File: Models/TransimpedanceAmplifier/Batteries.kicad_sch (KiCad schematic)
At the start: 8 parts

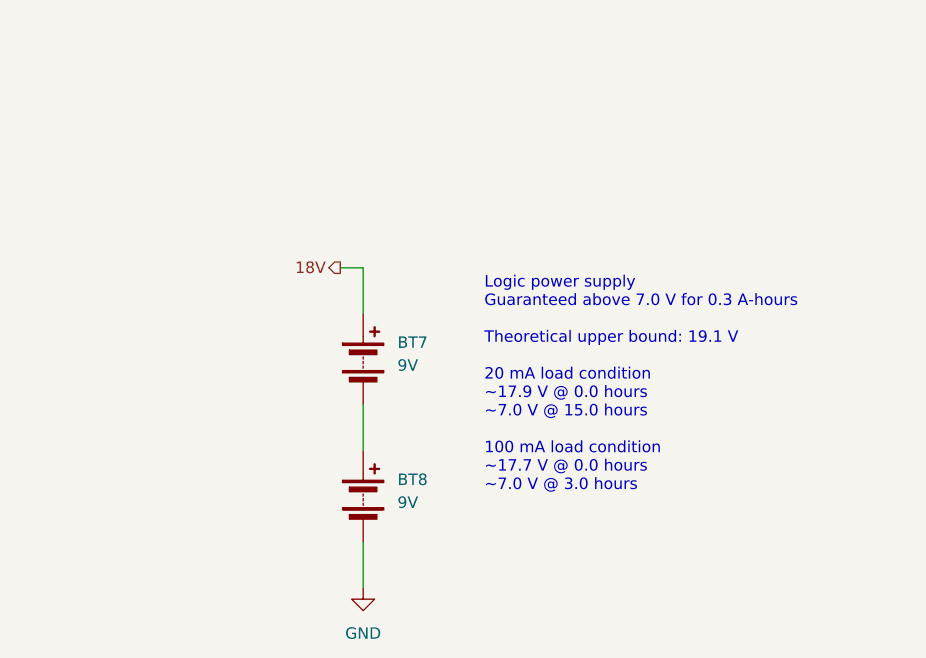
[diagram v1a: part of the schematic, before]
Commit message: Corrected some errors in the power calculations
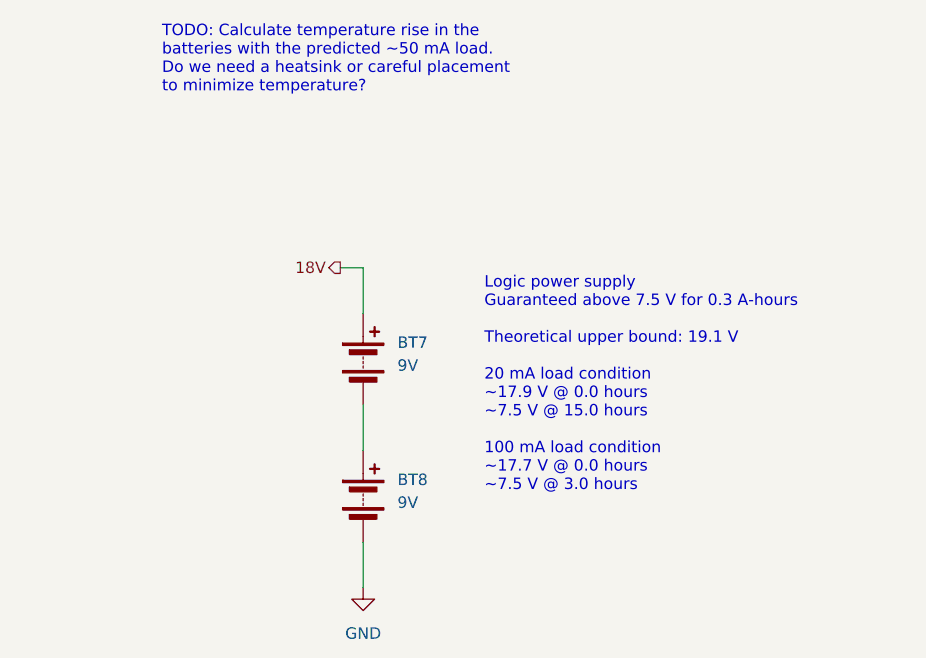
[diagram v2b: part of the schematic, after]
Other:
- note added: "Logic power supply Guaranteed above 7.5 V for 0.3 A-hours Theoretical upper bound: 19.1 V 20 mA load condition ~17.9 V @ 0.0 hours ~7.5 V @ 15.0 hours 100 mA load condition ~17.7 V @ 0.0 hours ~7.5 V @ 3.0 hours"
- note added: "TODO: Calculate temperature rise in the batteries with the predicted ~50 mA load. Do we need a heatsink or careful placement to minimize temperature?"
- note removed: "Logic power supply Guaranteed above 7.0 V for 0.3 A-hours Theoretical upper bound: 19.1 V 20 mA load condition ~17.9 V @ 0.0 hours ~7.0 V @ 15.0 hours 100 mA load condition ~17.7 V @ 0.0 hours ~7.0 V @ 3.0 hours"
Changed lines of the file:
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@@
 		)
 	)
-	(text "Logic power supply\nGuaranteed above 7.0 V for 0.3 A-hours\n\nTheoretical upper bound: 19.1 V\n\n20 mA load condition\n~17.9 V @ 0.0 hours\n~7.0 V @ 15.0 hours\n\n100 mA load condition\n~17.7 V @ 0.0 hours\n~7.0 V @ 3.0 hours"
+	(text "TODO: Calculate temperature rise in the\nbatteries with the predicted ~50 mA load.\nDo we need a heatsink or careful placement\nto minimize temperature?"
+		(exclude_from_sim no)
+		(at 142.748 39.116 0)
+		(effects
+			(font
+				(size 1.27 1.27)
+			)
+			(justify left top)
+		)
+	)
+	(text "Logic power supply\nGuaranteed above 7.5 V for 0.3 A-hours\n\nTheoretical upper bound: 19.1 V\n\n20 mA load condition\n~17.9 V @ 0.0 hours\n~7.5 V @ 15.0 hours\n\n100 mA load condition\n~17.7 V @ 0.0 hours\n~7.5 V @ 3.0 hours"
 		(exclude_from_sim no)
 		(at 178.562 67.056 0)

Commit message: Save progress
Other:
- note added: "Power / Thermal Concerns Internal resistance: 1-2 Ω per battery Maximum current load: 50 mA I2R power dissipation: 5 mW per battery"
- note removed: "TODO: Calculate temperature rise in the batteries with the predicted ~50 mA load. Do we need a heatsink or careful placement to minimize temperature?"
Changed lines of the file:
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@@
 		)
 	)
-	(text "TODO: Calculate temperature rise in the\nbatteries with the predicted ~50 mA load.\nDo we need a heatsink or careful placement\nto minimize temperature?"
+	(text "Logic power supply\nGuaranteed above 7.5 V for 0.3 A-hours\n\nTheoretical upper bound: 19.1 V\n\n20 mA load condition\n~17.9 V @ 0.0 hours\n~7.5 V @ 15.0 hours\n\n100 mA load condition\n~17.7 V @ 0.0 hours\n~7.5 V @ 3.0 hours"
 		(exclude_from_sim no)
-		(at 142.748 39.116 0)
+		(at 178.562 67.056 0)
 		(effects
 			(font
@@
 		)
 	)
-	(text "Logic power supply\nGuaranteed above 7.5 V for 0.3 A-hours\n\nTheoretical upper bound: 19.1 V\n\n20 mA load condition\n~17.9 V @ 0.0 hours\n~7.5 V @ 15.0 hours\n\n100 mA load condition\n~17.7 V @ 0.0 hours\n~7.5 V @ 3.0 hours"
+	(text "Power / Thermal Concerns\n\nInternal resistance: 1-2 Ω per battery\nMaximum current load: 50 mA\nI2R power dissipation: 5 mW per battery"
 		(exclude_from_sim no)
-		(at 178.562 67.056 0)
+		(at 152.908 26.67 0)
 		(effects
 			(font

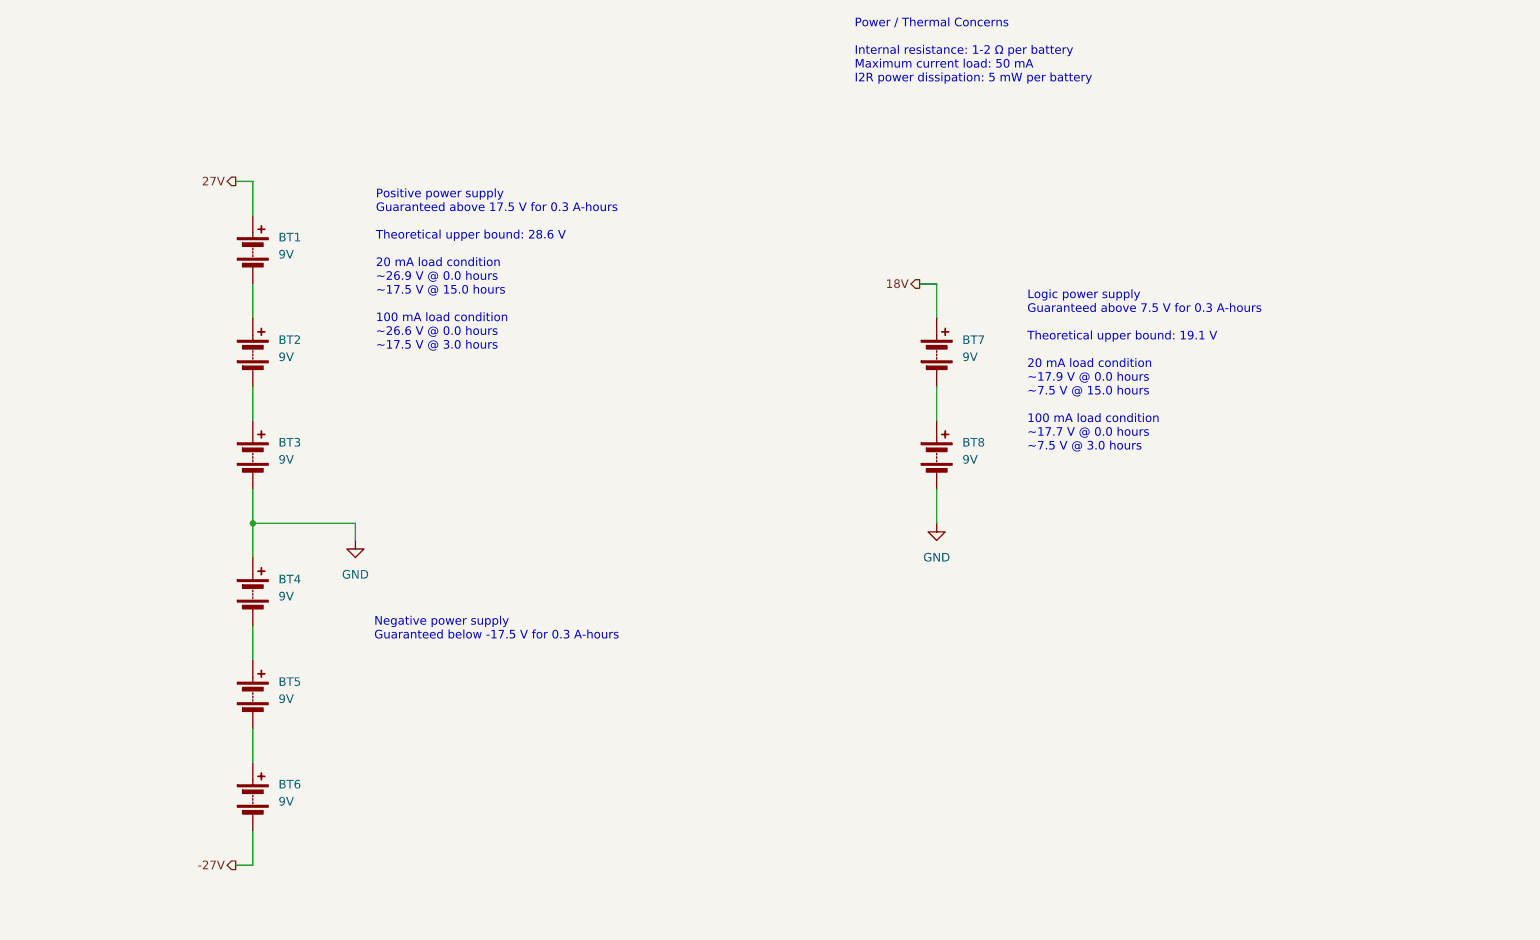
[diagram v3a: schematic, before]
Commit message: Improved the power supply schematic
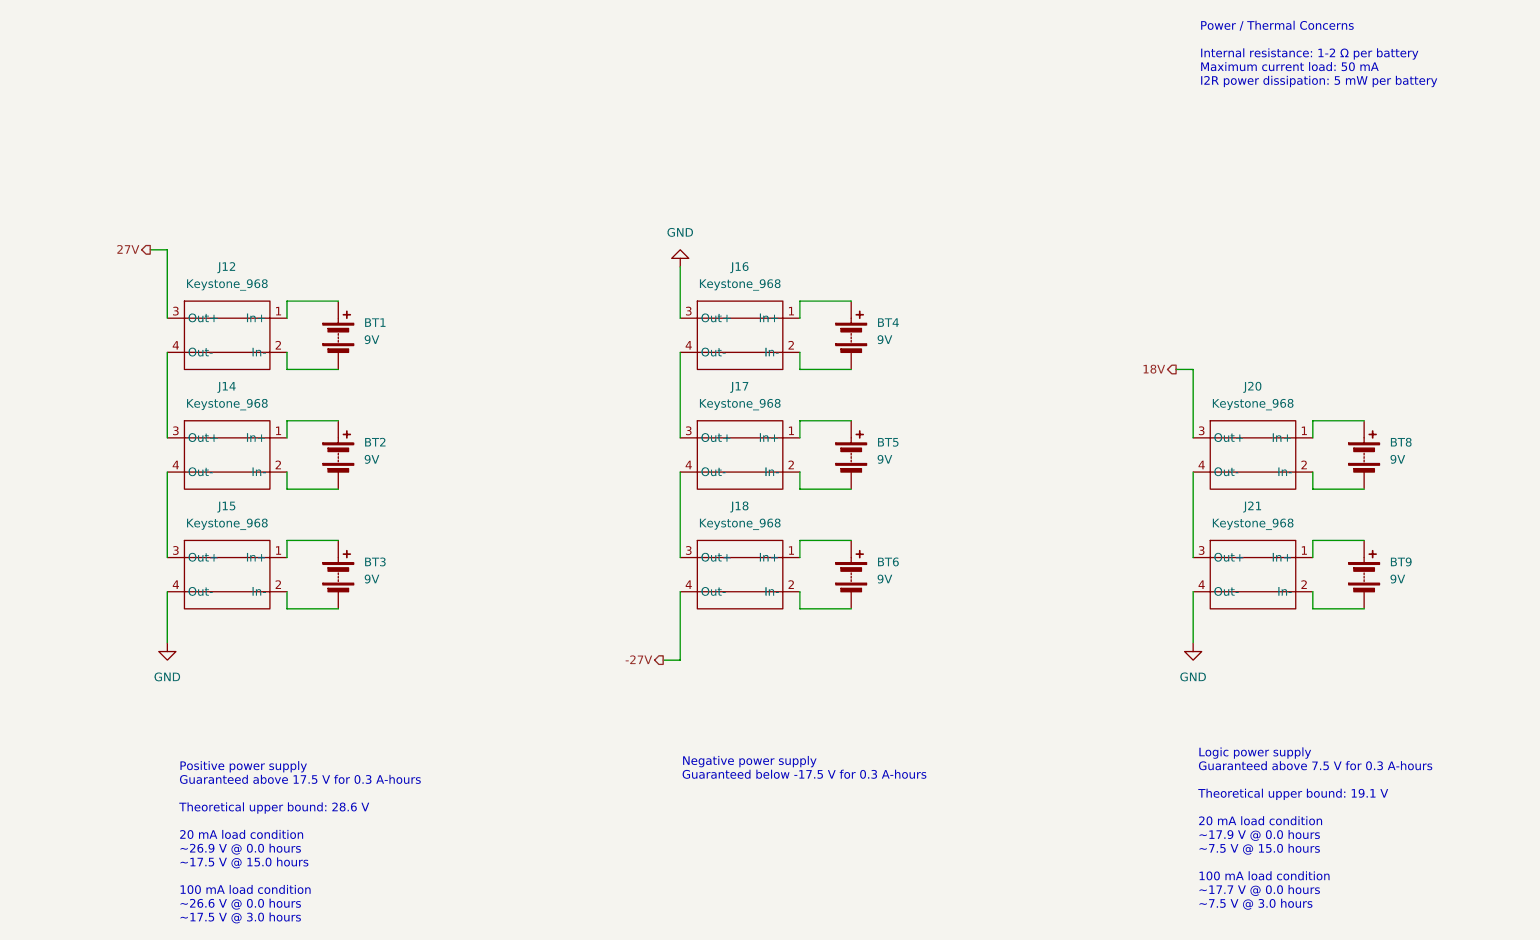
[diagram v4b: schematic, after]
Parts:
- removed BT7: 9V, symbol Device:Battery
- added BT9: 9V, symbol Device:Battery
- added J12, J14, J15, J16, J17, J18, J20, J21: Keystone_968, symbol Custom:Keystone_968
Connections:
- net -27V: now also J18.4 (Out-); no longer BT6.2 (-)
- net 18V: now also J20.3 (Out+)
- net 27V: now also J12.3 (Out+); no longer BT1.1 (+)
- net GND: now also J15.4 (Out-), J16.3 (Out+), J21.4 (Out-); no longer BT3.2 (-), BT4.1 (+), BT8.2 (-)
- net at BT5.1 (+): now also J17.1 (In+); no longer BT4.2 (-)
- net at BT5.2 (-): now also J17.2 (In-); no longer BT6.1 (+)
- net at BT8.1 (+): now also J20.1 (In+)
- net at BT1.2 (-): now also J12.2 (In-); no longer BT2.1 (+)
- net at BT2.2 (-): now also J14.2 (In-); no longer BT3.1 (+)
- new net: BT1.1 (+), J12.1 (In+)
- new net: J12.4 (Out-), J14.3 (Out+)
- new net: BT8.2 (-), J20.2 (In-)
- new net: BT2.1 (+), J14.1 (In+)
- new net: J14.4 (Out-), J15.3 (Out+)
- new net: BT4.1 (+), J16.1 (In+)
- new net: BT4.2 (-), J16.2 (In-)
- new net: J16.4 (Out-), J17.3 (Out+)
- new net: BT9.1 (+), J21.1 (In+)
- new net: BT9.2 (-), J21.2 (In-)
- new net: J20.4 (Out-), J21.3 (Out+)
- new net: BT3.1 (+), J15.1 (In+)
- new net: BT3.2 (-), J15.2 (In-)
- new net: J17.4 (Out-), J18.3 (Out+)
- new net: BT6.1 (+), J18.1 (In+)
- new net: BT6.2 (-), J18.2 (In-)

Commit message: Save progress
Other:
- note added: "TODO: Check that 9V batteries can be disconnected from their respective connectors with low force. TODO: Resolve issues with connectivity of the Keystone 968 footprints. Exclude the battery symbols from the board (they have no footprint)."
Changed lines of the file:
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@@
+		)
+	)
+	(text "TODO: Check that 9V batteries can be disconnected\nfrom their respective connectors with low force.\n\nTODO: Resolve issues with connectivity of\nthe Keystone 968 footprints. Exclude the battery\nsymbols from the board (they have no footprint)."
+		(exclude_from_sim no)
+		(at 43.434 29.21 0)
+		(effects
+			(font
+				(size 1.27 1.27)
+			)
+			(justify left top)
 		)
 	)
